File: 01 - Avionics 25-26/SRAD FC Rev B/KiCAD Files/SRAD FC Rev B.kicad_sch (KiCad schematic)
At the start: 0 parts

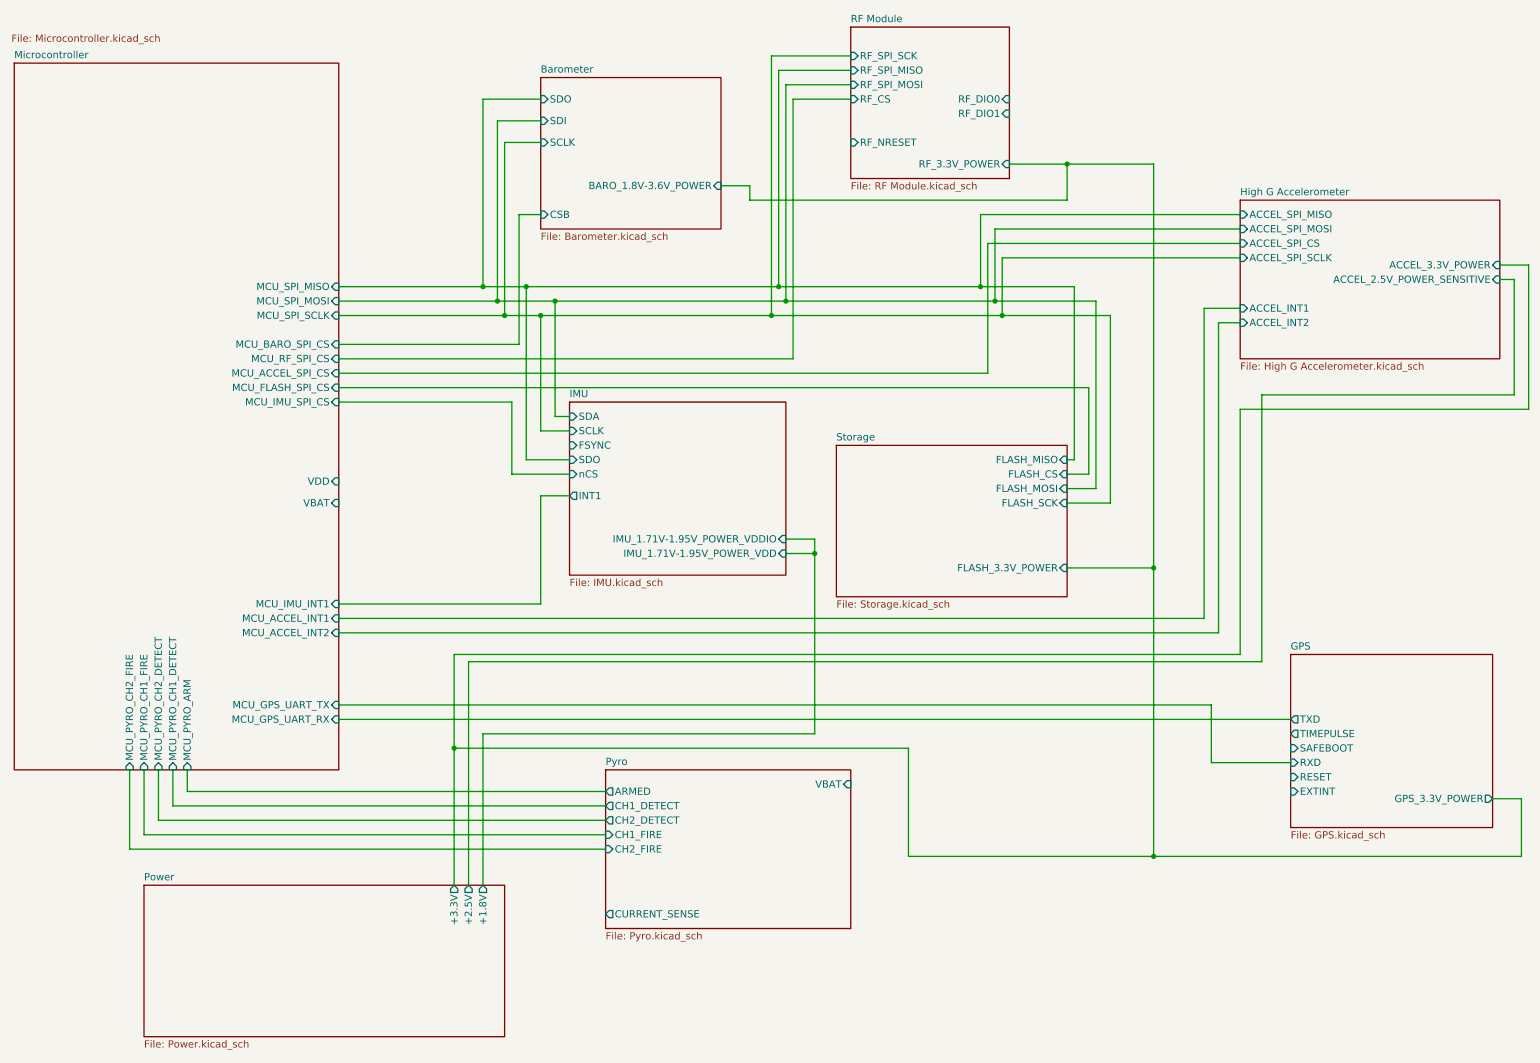
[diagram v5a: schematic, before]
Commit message: wired pyro current sense, rearranged some stuff
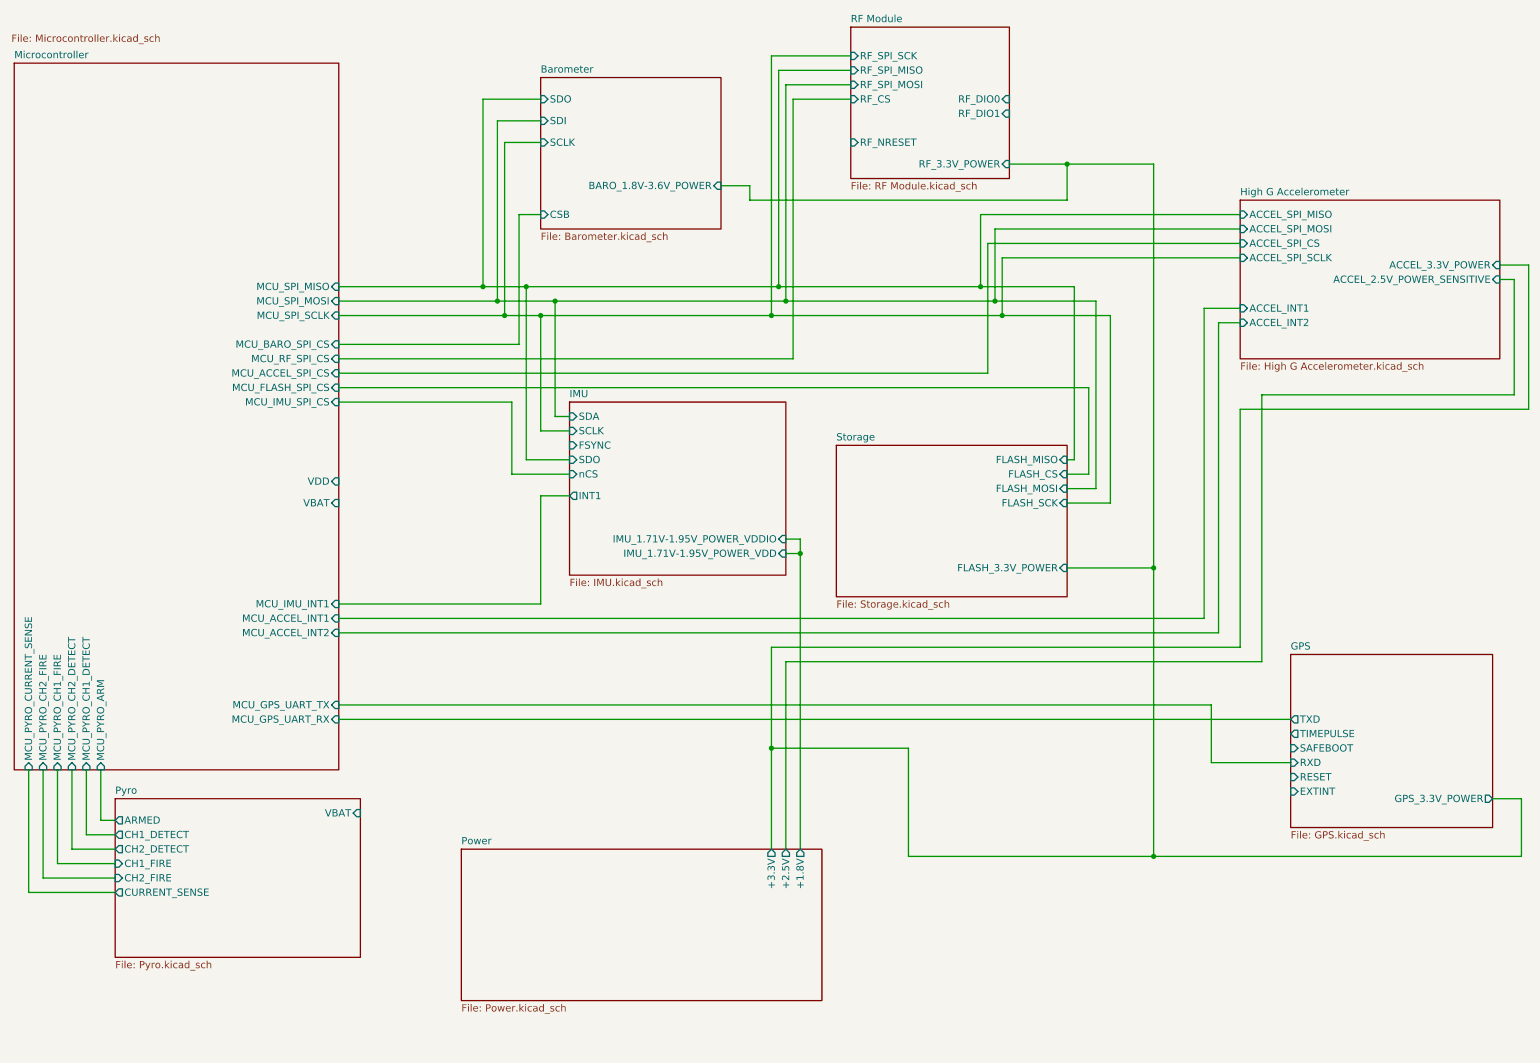
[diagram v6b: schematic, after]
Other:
- sheet Microcontroller ports: added MCU_PYRO_CURRENT_SENSE; removed none
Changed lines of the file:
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@@
 	)
 	(junction
-		(at 91.44 143.51)
+		(at 152.4 109.22)
 		(diameter 0)
 		(color 0 0 0 0)
@@
 	)
 	(junction
-		(at 154.94 109.22)
+		(at 187.96 67.31)
 		(diameter 0)
 		(color 0 0 0 0)
 	)
 	(junction
-		(at 187.96 67.31)
+		(at 147.32 143.51)
 		(diameter 0)
 		(color 0 0 0 0)
@@
 	(wire
 		(pts
-			(xy 154.94 140.97) (xy 154.94 109.22)
-		)
-		(stroke
-			(width 0)
-			(type default)
-		)
-	)
-	(wire
-		(pts
 			(xy 185.42 77.47) (xy 185.42 54.61)
 		)
@@
 	(wire
 		(pts
-			(xy 44.45 151.13) (xy 118.11 151.13)
-		)
-		(stroke
-			(width 0)
-			(type default)
-		)
-	)
-	(wire
-		(pts
-			(xy 93.98 167.64) (xy 93.98 128.27)
+			(xy 29.21 156.21) (xy 31.75 156.21)
+		)
+		(stroke
+			(width 0)
+			(type default)
+		)
+	)
+	(wire
+		(pts
+			(xy 149.86 161.29) (xy 149.86 128.27)
 		)
 		(stroke
@@
 	(wire
 		(pts
-			(xy 96.52 140.97) (xy 154.94 140.97)
-		)
-		(stroke
-			(width 0)
-			(type default)
-		)
-	)
-	(wire
-		(pts
 			(xy 106.68 99.06) (xy 111.76 99.06)
 		)
@@
 	(wire
 		(pts
-			(xy 96.52 167.64) (xy 96.52 140.97)
+			(xy 152.4 109.22) (xy 152.4 161.29)
 		)
 		(stroke
@@
 	(wire
 		(pts
+			(xy 147.32 125.73) (xy 147.32 143.51)
+		)
+		(stroke
+			(width 0)
+			(type default)
+		)
+	)
+	(wire
+		(pts
 			(xy 109.22 85.09) (xy 111.76 85.09)
 		)
@@
 	(wire
 		(pts
-			(xy 36.83 147.32) (xy 36.83 158.75)
+			(xy 21.59 147.32) (xy 21.59 163.83)
+		)
+		(stroke
+			(width 0)
+			(type default)
+		)
+	)
+	(wire
+		(pts
+			(xy 16.51 147.32) (xy 16.51 168.91)
 		)
 		(stroke
@@
 	(wire
 		(pts
-			(xy 171.45 143.51) (xy 91.44 143.51)
-		)
-		(stroke
-			(width 0)
-			(type default)
-		)
-	)
-	(wire
-		(pts
-			(xy 91.44 143.51) (xy 91.44 127)
-		)
-		(stroke
-			(width 0)
-			(type default)
-		)
-	)
-	(wire
-		(pts
 			(xy 147.32 67.31) (xy 147.32 21.59)
 		)
@@
 	(wire
 		(pts
-			(xy 36.83 158.75) (xy 118.11 158.75)
+			(xy 21.59 163.83) (xy 31.75 163.83)
 		)
 		(stroke
@@
 	(wire
 		(pts
-			(xy 39.37 156.21) (xy 118.11 156.21)
+			(xy 24.13 161.29) (xy 31.75 161.29)
 		)
 		(stroke
@@
 	(wire
 		(pts
-			(xy 154.94 109.22) (xy 149.86 109.22)
-		)
-		(stroke
-			(width 0)
-			(type default)
-		)
-	)
-	(wire
-		(pts
 			(xy 199.39 40.64) (xy 199.39 46.99)
 		)
@@
 	(wire
 		(pts
-			(xy 34.29 161.29) (xy 118.11 161.29)
+			(xy 19.05 166.37) (xy 31.75 166.37)
 		)
 		(stroke
@@
 	(wire
 		(pts
-			(xy 149.86 106.68) (xy 154.94 106.68)
+			(xy 149.86 106.68) (xy 152.4 106.68)
 		)
 		(stroke
@@
 	(wire
 		(pts
-			(xy 44.45 147.32) (xy 44.45 151.13)
+			(xy 29.21 147.32) (xy 29.21 156.21)
 		)
 		(stroke
@@
 	(wire
 		(pts
-			(xy 154.94 106.68) (xy 154.94 109.22)
-		)
-		(stroke
-			(width 0)
-			(type default)
-		)
-	)
-	(wire
-		(pts
-			(xy 91.44 143.51) (xy 91.44 167.64)
+			(xy 152.4 106.68) (xy 152.4 109.22)
+		)
+		(stroke
+			(width 0)
+			(type default)
+		)
+	)
+	(wire
+		(pts
+			(xy 147.32 143.51) (xy 147.32 161.29)
 		)
 		(stroke
@@
 	(wire
 		(pts
-			(xy 41.91 153.67) (xy 118.11 153.67)
+			(xy 26.67 158.75) (xy 31.75 158.75)
 		)
 		(stroke
@@
 	(wire
 		(pts
-			(xy 91.44 127) (xy 229.87 127)
+			(xy 147.32 125.73) (xy 229.87 125.73)
+		)
+		(stroke
+			(width 0)
+			(type default)
+		)
+	)
+	(wire
+		(pts
+			(xy 147.32 143.51) (xy 171.45 143.51)
+		)
+		(stroke
+			(width 0)
+			(type default)
+		)
+	)
+	(wire
+		(pts
+			(xy 152.4 109.22) (xy 149.86 109.22)
 		)
 		(stroke
@@
 	(wire
 		(pts
-			(xy 93.98 128.27) (xy 233.68 128.27)
-		)
-		(stroke
-			(width 0)
-			(type default)
-		)
-	)
-	(wire
-		(pts
-			(xy 34.29 147.32) (xy 34.29 161.29)
+			(xy 149.86 128.27) (xy 233.68 128.27)
+		)
+		(stroke
+			(width 0)
+			(type default)
+		)
+	)
+	(wire
+		(pts
+			(xy 19.05 147.32) (xy 19.05 166.37)
 		)
 		(stroke
@@
 	(wire
 		(pts
-			(xy 39.37 147.32) (xy 39.37 156.21)
-		)
-		(stroke
-			(width 0)
-			(type default)
-		)
-	)
-	(wire
-		(pts
-			(xy 229.87 127) (xy 229.87 83.82)
+			(xy 24.13 147.32) (xy 24.13 161.29)
+		)
+		(stroke
+			(width 0)
+			(type default)
+		)
+	)
+	(wire
+		(pts
+			(xy 229.87 125.73) (xy 229.87 83.82)
 		)
 		(stroke
@@
 	(wire
 		(pts
+			(xy 16.51 168.91) (xy 31.75 168.91)
+		)
+		(stroke
+			(width 0)
+			(type default)
+		)
+	)
+	(wire
+		(pts
 			(xy 147.32 67.31) (xy 187.96 67.31)
 		)
@@
 	(wire
 		(pts
-			(xy 41.91 147.32) (xy 41.91 153.67)
+			(xy 26.67 147.32) (xy 26.67 158.75)
 		)
 		(stroke
@@
 	)
 	(sheet
-		(at 36.83 167.64)
+		(at 92.71 161.29)
 		(size 63.5 26.67)
 		(exclude_from_sim no)
@@
 		)
 		(property "Sheetname" "Power"
-			(at 36.83 166.9284 0)
+			(at 92.71 160.5784 0)
 			(effects
 				(font
@@
 		)
 		(property "Sheetfile" "Power.kicad_sch"
-			(at 36.83 194.8946 0)
+			(at 92.71 188.5446 0)
 			(effects
 				(font
@@
 		)
 		(pin "+1.8V" output
-			(at 96.52 167.64 90)
+			(at 152.4 161.29 90)
 			(effects
 				(font
@@
 		)
 		(pin "+2.5V" output
-			(at 93.98 167.64 90)
+			(at 149.86 161.29 90)
 			(effects
 				(font
@@
 		)
 		(pin "+3.3V" output
-			(at 91.44 167.64 90)
+			(at 147.32 161.29 90)
 			(effects
 				(font
@@
 		)
 		(pin "MCU_PYRO_CH2_FIRE" input
-			(at 34.29 147.32 270)
+			(at 19.05 147.32 270)
 			(effects
 				(font
@@
 		)
 		(pin "MCU_PYRO_CH2_DETECT" input
-			(at 39.37 147.32 270)
+			(at 24.13 147.32 270)
 			(effects
 				(font
@@
 		)
 		(pin "MCU_PYRO_ARM" input
-			(at 44.45 147.32 270)
+			(at 29.21 147.32 270)
 			(effects
 				(font
@@
 		)
 		(pin "MCU_PYRO_CH1_FIRE" input
-			(at 36.83 147.32 270)
+			(at 21.59 147.32 270)
 			(effects
 				(font
@@
 		)
 		(pin "MCU_PYRO_CH1_DETECT" input
-			(at 41.91 147.32 270)
+			(at 26.67 147.32 270)
+			(effects
+				(font
+					(size 1.27 1.27)
+				)
+				(justify left)
+			)
+		)
+		(pin "MCU_PYRO_CURRENT_SENSE" input
+			(at 16.51 147.32 270)
 			(effects
 				(font
@@
 	)
 	(sheet
-		(at 118.11 147.32)
+		(at 31.75 152.4)
 		(size 43.18 27.94)
 		(exclude_from_sim no)
@@
 		)
 		(property "Sheetname" "Pyro"
-			(at 118.11 146.6084 0)
+			(at 31.75 151.6884 0)
 			(effects
 				(font
@@
 		)
 		(property "Sheetfile" "Pyro.kicad_sch"
-			(at 118.11 175.8446 0)
+			(at 31.75 180.9246 0)
 			(effects
 				(font
@@
 		)
 		(pin "CURRENT_SENSE" output
-			(at 118.11 172.72 180)
+			(at 31.75 168.91 180)
 			(effects
 				(font
@@
 		)
 		(pin "CH1_DETECT" output
-			(at 118.11 153.67 180)
+			(at 31.75 158.75 180)
 			(effects
 				(font
@@
 		)
 		(pin "CH2_DETECT" output
-			(at 118.11 156.21 180)
+			(at 31.75 161.29 180)
 			(effects
 				(font
@@
 		)
 		(pin "CH1_FIRE" input
-			(at 118.11 158.75 180)
+			(at 31.75 163.83 180)
 			(effects
 				(font
@@
 		)
 		(pin "ARMED" output
-			(at 118.11 151.13 180)
+			(at 31.75 156.21 180)
 			(effects
 				(font
@@
 		)
 		(pin "CH2_FIRE" input
-			(at 118.11 161.29 180)
+			(at 31.75 166.37 180)
 			(effects
 				(font
@@
 		)
 		(pin "VBAT" input
-			(at 161.29 149.86 0)
-			(effects
-				(font
+			(at 74.93 154.94 0)
+			(effects
+				(font

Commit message: added some more wiring for GPS
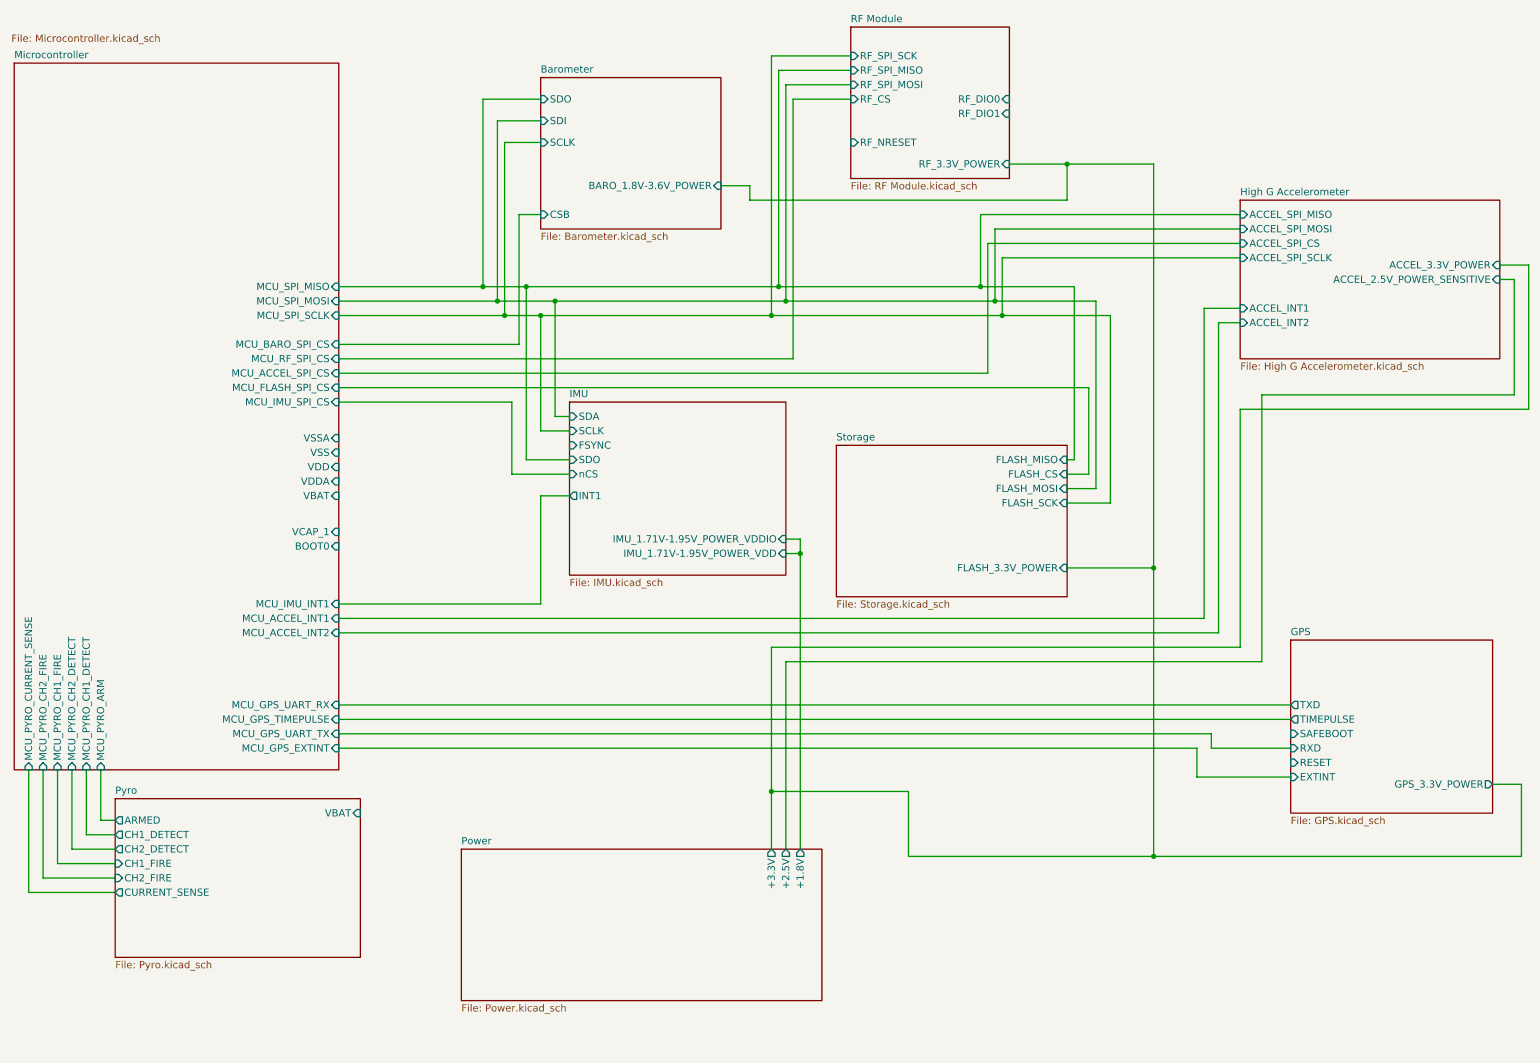
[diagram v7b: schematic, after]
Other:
- sheet Microcontroller ports: added BOOT0, MCU_GPS_EXTINT, MCU_GPS_TIMEPULSE, VCAP_1, VDDA, VSS, VSSA; removed none
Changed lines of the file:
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@@
+	)
+	(junction
+		(at 147.32 151.13)
+		(diameter 0)
+		(color 0 0 0 0)
 	)
 	(junction
@@
 	)
 	(junction
-		(at 147.32 143.51)
-		(diameter 0)
-		(color 0 0 0 0)
-	)
-	(junction
 		(at 214.63 111.76)
 		(diameter 0)
@@
 	(wire
 		(pts
+			(xy 147.32 151.13) (xy 147.32 161.29)
+		)
+		(stroke
+			(width 0)
+			(type default)
+		)
+	)
+	(wire
+		(pts
 			(xy 185.42 54.61) (xy 229.87 54.61)
 		)
@@
 	(wire
 		(pts
-			(xy 147.32 125.73) (xy 147.32 143.51)
+			(xy 147.32 125.73) (xy 147.32 151.13)
 		)
 		(stroke
@@
 	(wire
 		(pts
-			(xy 224.79 146.05) (xy 238.76 146.05)
+			(xy 224.79 143.51) (xy 238.76 143.51)
 		)
 		(stroke
@@
 	(wire
 		(pts
+			(xy 71.12 135.89) (xy 238.76 135.89)
+		)
+		(stroke
+			(width 0)
+			(type default)
+		)
+	)
+	(wire
+		(pts
 			(xy 102.87 49.53) (xy 106.68 49.53)
 		)
@@
 	(wire
 		(pts
-			(xy 224.79 135.89) (xy 224.79 146.05)
+			(xy 224.79 140.97) (xy 224.79 143.51)
 		)
 		(stroke
@@
 	(wire
 		(pts
+			(xy 71.12 138.43) (xy 238.76 138.43)
+		)
+		(stroke
+			(width 0)
+			(type default)
+		)
+	)
+	(wire
+		(pts
 			(xy 186.69 64.77) (xy 204.47 64.77)
 		)
@@
 	(wire
 		(pts
-			(xy 71.12 138.43) (xy 238.76 138.43)
-		)
-		(stroke
-			(width 0)
-			(type default)
-		)
-	)
-	(wire
-		(pts
 			(xy 24.13 161.29) (xy 31.75 161.29)
 		)
@@
 	(wire
 		(pts
-			(xy 279.4 152.4) (xy 279.4 162.56)
+			(xy 279.4 149.86) (xy 279.4 162.56)
 		)
 		(stroke
@@
 	(wire
 		(pts
+			(xy 71.12 143.51) (xy 222.25 143.51)
+		)
+		(stroke
+			(width 0)
+			(type default)
+		)
+	)
+	(wire
+		(pts
 			(xy 104.14 62.23) (xy 104.14 92.71)
 		)
@@
 	(wire
 		(pts
-			(xy 147.32 143.51) (xy 147.32 161.29)
-		)
-		(stroke
-			(width 0)
-			(type default)
-		)
-	)
-	(wire
-		(pts
 			(xy 280.67 83.82) (xy 280.67 58.42)
 		)
@@
 	(wire
 		(pts
-			(xy 71.12 135.89) (xy 224.79 135.89)
-		)
-		(stroke
-			(width 0)
-			(type default)
-		)
-	)
-	(wire
-		(pts
-			(xy 274.32 152.4) (xy 279.4 152.4)
+			(xy 71.12 140.97) (xy 224.79 140.97)
+		)
+		(stroke
+			(width 0)
+			(type default)
+		)
+	)
+	(wire
+		(pts
+			(xy 274.32 149.86) (xy 279.4 149.86)
 		)
 		(stroke
@@
 	(wire
 		(pts
-			(xy 171.45 162.56) (xy 171.45 143.51)
+			(xy 171.45 162.56) (xy 171.45 151.13)
 		)
 		(stroke
@@
 	(wire
 		(pts
-			(xy 147.32 143.51) (xy 171.45 143.51)
+			(xy 147.32 151.13) (xy 171.45 151.13)
 		)
 		(stroke
@@
 	(wire
 		(pts
+			(xy 222.25 148.59) (xy 238.76 148.59)
+		)
+		(stroke
+			(width 0)
+			(type default)
+		)
+	)
+	(wire
+		(pts
 			(xy 214.63 40.64) (xy 199.39 40.64)
 		)
@@
 		(pts
 			(xy 24.13 147.32) (xy 24.13 161.29)
+		)
+		(stroke
+			(width 0)
+			(type default)
+		)
+	)
+	(wire
+		(pts
+			(xy 222.25 143.51) (xy 222.25 148.59)
 		)
 		(stroke
@@
 		)
 		(pin "VBAT" input
-			(at 71.12 100.33 0)
+			(at 71.12 99.06 0)
 			(effects
 				(font
@@
 		)
 		(pin "VDD" input
-			(at 71.12 96.52 0)
+			(at 71.12 93.98 0)
 			(effects
 				(font
@@
 		)
 		(pin "MCU_GPS_UART_RX" input
-			(at 71.12 138.43 0)
+			(at 71.12 135.89 0)
 			(effects
 				(font
@@
 		)
 		(pin "MCU_GPS_UART_TX" input
-			(at 71.12 135.89 0)
+			(at 71.12 140.97 0)
 			(effects
 				(font
@@
 				)
 				(justify left)
+			)
+		)
+		(pin "VSS" input
+			(at 71.12 91.44 0)
+			(effects
+				(font
+					(size 1.27 1.27)
+				)
+				(justify right)
+			)
+		)
+		(pin "VDDA" input
+			(at 71.12 96.52 0)
+			(effects
+				(font
+					(size 1.27 1.27)
+				)
+				(justify right)
+			)
+		)
+		(pin "VSSA" input
+			(at 71.12 88.9 0)
+			(effects
+				(font
+					(size 1.27 1.27)
+				)
+				(justify right)
+			)
+		)
+		(pin "VCAP_1" input
+			(at 71.12 105.41 0)
+			(effects
+				(font
+					(size 1.27 1.27)
+				)
+				(justify right)
+			)
+		)
+		(pin "MCU_GPS_EXTINT" input
+			(at 71.12 143.51 0)
+			(effects
+				(font
+					(size 1.27 1.27)
+				)
+				(justify right)
+			)
+		)
+		(pin "MCU_GPS_TIMEPULSE" input
+			(at 71.12 138.43 0)
+			(effects
+				(font
+					(size 1.27 1.27)
+				)
+				(justify right)
+			)
+		)
+		(pin "BOOT0" input
+			(at 71.12 107.95 0)
+			(effects
+				(font
+					(size 1.27 1.27)
+				)
+				(justify right)
 			)
 		)
@@
 	)
 	(sheet
-		(at 238.76 127)
+		(at 238.76 124.46)
 		(size 35.56 30.48)
 		(exclude_from_sim no)
@@
 		)
 		(property "Sheetname" "GPS"
-			(at 238.76 126.2884 0)
+			(at 238.76 123.7484 0)
 			(effects
 				(font
@@
 		)
 		(property "Sheetfile" "GPS.kicad_sch"
-			(at 238.76 158.0646 0)
+			(at 238.76 155.5246 0)
 			(effects
 				(font
@@
 		)
 		(pin "EXTINT" input
-			(at 238.76 151.13 180)
+			(at 238.76 148.59 180)
 			(effects
 				(font
@@
 		)
 		(pin "RESET" input
-			(at 238.76 148.59 180)
+			(at 238.76 146.05 180)
 			(effects
 				(font
@@
 		)
 		(pin "RXD" input
-			(at 238.76 146.05 180)
+			(at 238.76 143.51 180)
 			(effects
 				(font
@@
 		)
 		(pin "SAFEBOOT" input
-			(at 238.76 143.51 180)
+			(at 238.76 140.97 180)
 			(effects
 				(font
@@
 		)
 		(pin "TIMEPULSE" output
-			(at 238.76 140.97 180)
+			(at 238.76 138.43 180)
 			(effects
 				(font
@@
 		)
 		(pin "TXD" output
-			(at 238.76 138.43 180)
+			(at 238.76 135.89 180)
 			(effects
 				(font
@@
 		)
 		(pin "GPS_3.3V_POWER" output
-			(at 274.32 152.4 0)
-			(effects
-				(font
+			(at 274.32 149.86 0)
+			(effects
+				(font
